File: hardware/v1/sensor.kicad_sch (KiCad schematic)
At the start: 22 parts, among them J10 Conn_01x03, J11 Conn_01x03, J3 Conn_01x03, J6 Conn_01x03, J7 Conn_01x03, J9 Conn_01x03, Q2 MMBT3904, U4 PCA9685BS, U5 BMI088, U7 BMP388

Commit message: some hardware designs
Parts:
- added C14, C15: 100n, Capacitor_SMD:C_0402_1005Metric, symbol Device:C
- added C15: 1u, Capacitor_SMD:C_0402_1005Metric, symbol Device:C
- added C26: 10n, Capacitor_SMD:C_0402_1005Metric, symbol Device:C_Small
- added J8: Conn_Coaxial, Connector_Coaxial:U.FL_Molex_MCRF_73412-0110_Vertical, symbol Connector:Conn_Coaxial
- added L1: L_Small, Inductor_SMD:L_0603_1608Metric, symbol Device:L_Small
- added R19: 10, Resistor_SMD:R_0402_1005Metric, symbol Device:R_Small
- added SW4: ACT/PASS, Button_Switch_SMD:SW_SPDT_PCM12, symbol Switch:SW_SPDT
- added U4: LIS3MDL, Package_LGA:LGA-12_2x2mm_P0.5mm, symbol Sensor_Magnetic:LIS3MDL
- added U8: NEO-M8N, RF_GPS:ublox_NEO, symbol RF_GPS:NEO-M8N
- U5: footprint LCSC:LGA-16_L4.5-W3.0-P0.50-BL -> ollyfc:PQFN50P450X300X100-16N
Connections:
- net +3V3: now also C15.1, C15.1, U4.5 (Vdd), U4.6 (Vdd_IO), U8.23 (VCC)
- net GND: now also C14.2, C15.2, C15.2, C26.2, J8.2 (Ext), U4.12 (GND), U4.2 (GND), U4.3 (GND), U8.10 (GND), U8.12 (GND), U8.13 (GND), U8.2 (D_SEL), U8.24 (GND), U8.7 (VDD_USB)
- net SPI2_MISO: now also U4.9 (SDO/SA1), U8.20 (TXD/SPI_MISO)
- net SPI2_MOSI: now also U4.11 (SDA/SDI/SDO), U8.21 (RXD/SPI_MOSI)
- net SPI2_SCK: now also U4.1 (SCL/SPC), U8.19 (SCL/SPI_CLK)
- new net: C26.1, L1.1, R19.2
- new net: C14.1, U4.4 (C1)
- new net: SW4.2 (B), U8.9 (VCC_RF)
- new net: R19.1, SW4.3 (C)
- new net GNSS_CS: U8.18 (SDA/~{SPI_CS})
- new net GNSS_INT: U8.4 (EXTINT)
- new net GNSS_RESET: U8.8 (~{RESET})
- new net GNSS_SAFEBOOT: U8.1 (~{SAFEBOOT})
- new net GNSS_TIMEP: U8.3 (TIMEPULSE)
- new net LNA_EN: U8.14 (LNA_EN)
- new net MAG_CS: U4.10 (~{CS})
- new net MAG_DRDY: U4.8 (DRDY)
- new net MAG_INT: U4.7 (INT)
- new net RF_IN: J8.1 (In), L1.2, U8.11 (RF_IN)
- new net VBAT: U8.22 (V_BCKP)
- no-connect marks 9 -> 11
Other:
- moved on the sheet: BZ1, C12, C13, C17, C18, D2, J10, J11, J3, J6, J7, J9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

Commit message: Route another?
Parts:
- removed SW4: ACT/PASS, Button_Switch_SMD:SW_SPDT_PCM12, symbol Switch:SW_SPDT
- added JP1: Jumper_2_Open, Connector_PinHeader_2.54mm:PinHeader_1x02_P2.54mm_Vertical, symbol Jumper:Jumper_2_Open
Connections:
- net CSB_ACCEL is gone; now on net +3V3: U5.14 (CSB1)
- net I2C3_SCL is gone; now on net I2C2_SCL: U4.23 (SCL)
- net I2C3_SDA is gone; now on net I2C2_SDA: U4.24 (SDA)
- net MAG_CS is gone; now on net +3V3: U4.10 (~{CS})
- net +3V3: now also U5.7 (PS)
- net 5VIN: now also BZ1.P (-); no longer BZ1.1 (-)
- net GND: now also U4.9 (SDO/SA1), U5.10 (SDO2), U5.15 (SDO1), U5.2 (NC); no longer U5.7 (PS), U8.2 (D_SEL)
- net SERVO_CH4: now also U4.15 (LED11); no longer U4.17 (LED13)
- net SERVO_CH5: now also U4.16 (LED12); no longer U4.18 (LED14)
- net SERVO_CH6: now also U4.17 (LED13); no longer U4.19 (LED15)
- net STATUS_A: now also U4.18 (LED14); no longer U4.9 (LED6)
- net STATUS_B: now also U4.19 (LED15); no longer U4.10 (LED7)
- net at C26.1, R19.2: now also JP1.2 (B); no longer L1.1
- net at U8.9 (VCC_RF): now also R19.1
- net at Q2.3 (C): now also BZ1.N (+); no longer BZ1.2 (+)
- net CSB_GYRO: no longer names the net of U5.5 (CSB2)
- net GNSS_CS renamed I2C1_SDA
- net I2C1_SDA: now also U4.11 (SDA/SDI/SDO), U5.9 (SDA/SDI)
- net LNA_EN: no longer names the net of U8.14 (LNA_EN)
- removed net SPI2_MISO: U4.9 (SDO/SA1), U5.10 (SDO2), U5.15 (SDO1), U8.20 (TXD/SPI_MISO)
- removed net SPI2_MOSI: U4.11 (SDA/SDI/SDO), U5.9 (SDA/SDI), U8.21 (RXD/SPI_MOSI)
- net SPI2_SCK renamed I2C1_SCL
- new net: JP1.1 (A), L1.1
- no-connect marks 11 -> 15
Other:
- moved on the sheet: C26, J10, J11, R19

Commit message: v2 PCB design
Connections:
- net VBAT is gone; now on net +3V3: U8.22 (V_BCKP)
- net I2C1_SCL: now also U7.2 (SCK); no longer U8.19 (SCL/SPI_CLK)
- net I2C1_SDA: now also U7.4 (SDI); no longer U8.18 (SDA/~{SPI_CS})
- net I2C2_SCL: now also U8.19 (SCL/SPI_CLK); no longer U7.2 (SCK)
- net I2C2_SDA: now also U8.18 (SDA/~{SPI_CS}); no longer U7.4 (SDI)
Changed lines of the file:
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@@
   (junction (at 32.385 162.56) (diameter 0) (color 0 0 0 0)
+  )
+  (junction (at 176.53 86.36) (diameter 0) (color 0 0 0 0)
   )
   (junction (at 82.55 45.72) (diameter 0) (color 0 0 0 0)
@@
     (stroke (width 0) (type default))
   )
-  (wire (pts (xy 179.07 89.535) (xy 179.07 77.47))
-    (stroke (width 0) (type default))
-  )
   (wire (pts (xy 79.375 134.62) (xy 69.85 134.62))
     (stroke (width 0) (type default))
@@
     (stroke (width 0) (type default))
   )
-  (wire (pts (xy 173.99 86.36) (xy 176.53 86.36))
-    (stroke (width 0) (type default))
-  )
   (wire (pts (xy 162.56 46.355) (xy 162.56 52.705))
     (stroke (width 0) (type default))
@@
     (stroke (width 0) (type default))
   )
+  (wire (pts (xy 179.07 89.535) (xy 179.07 86.36))
+    (stroke (width 0) (type default))
+  )
   (wire (pts (xy 258.445 27.94) (xy 256.54 27.94))
     (stroke (width 0) (type default))
@@
     (stroke (width 0) (type default))
   )
+  (wire (pts (xy 176.53 74.93) (xy 176.53 86.36))
+    (stroke (width 0) (type default))
+  )
   (wire (pts (xy 142.875 46.99) (xy 142.875 45.72))
     (stroke (width 0) (type default))
@@
     (stroke (width 0) (type default))
   )
-  (wire (pts (xy 179.07 77.47) (xy 175.895 77.47))
+  (wire (pts (xy 176.53 86.36) (xy 176.53 89.535))
     (stroke (width 0) (type default))
   )
@@
     (stroke (width 0) (type default))
   )
+  (wire (pts (xy 179.07 86.36) (xy 176.53 86.36))
+    (stroke (width 0) (type default))
+  )
   (wire (pts (xy 82.55 45.72) (xy 82.55 46.355))
     (stroke (width 0) (type default))
@@
   )
   (wire (pts (xy 242.57 41.91) (xy 248.92 41.91))
-    (stroke (width 0) (type default))
-  )
-  (wire (pts (xy 176.53 86.36) (xy 176.53 89.535))
     (stroke (width 0) (type default))
   )
@@
     )
   )
-  (global_label "I2C2_SDA" (shape input) (at 102.87 52.07 180) (fields_autoplaced)
+  (global_label "I2C1_SDA" (shape input) (at 102.87 52.07 180) (fields_autoplaced)
     (effects (font (size 1.27 1.27)) (justify right))
     (property "Intersheetrefs" "${INTERSHEET_REFS}" (at 91.0553 52.07 0)
@@
     )
   )
-  (global_label "I2C2_SCL" (shape input) (at 102.87 46.99 180) (fields_autoplaced)
+  (global_label "I2C1_SCL" (shape input) (at 102.87 46.99 180) (fields_autoplaced)
     (effects (font (size 1.27 1.27)) (justify right))
     (property "Intersheetrefs" "${INTERSHEET_REFS}" (at 91.1158 46.99 0)
@@
     )
   )
-  (global_label "I2C1_SDA" (shape input) (at 163.83 112.395 180) (fields_autoplaced)
+  (global_label "I2C2_SDA" (shape input) (at 163.83 112.395 180) (fields_autoplaced)
     (effects (font (size 1.27 1.27)) (justify right))
     (property "Intersheetrefs" "${INTERSHEET_REFS}" (at 152.0153 112.395 0)
@@
     )
   )
-  (global_label "I2C1_SCL" (shape input) (at 163.83 114.935 180) (fields_autoplaced)
+  (global_label "I2C2_SCL" (shape input) (at 163.83 114.935 180) (fields_autoplaced)
     (effects (font (size 1.27 1.27)) (justify right))
     (property "Intersheetrefs" "${INTERSHEET_REFS}" (at 152.0758 114.935 0)
-      (effects (font (size 1.27 1.27)) (justify right) hide)
-    )
-  )
-  (global_label "VBAT" (shape input) (at 175.895 77.47 180) (fields_autoplaced)
-    (effects (font (size 1.27 1.27)) (justify right))
-    (property "Intersheetrefs" "${INTERSHEET_REFS}" (at 168.495 77.47 0)
       (effects (font (size 1.27 1.27)) (justify right) hide)
     )
@@
       (effects (font (size 1.27 1.27)) (justify left))
     )
-    (property "Footprint" "ollyfc:PQFN50P450X300X100-16N" (at 53.34 72.39 0)
+    (property "Footprint" "ollyfc:PQFN50P450X300X100-16N" (at 53.34 59.69 0)
       (effects (font (size 1.27 1.27)))
     )
@@
     )
   )
-  (symbol (lib_id "power:+3V3") (at 173.99 86.36 0) (unit 1)
+  (symbol (lib_id "power:+3V3") (at 176.53 74.93 0) (unit 1)
     (in_bom yes) (on_board yes) (dnp no)
-    (property "Reference" "#PWR036" (at 173.99 90.17 0)
-      (effects (font (size 1.27 1.27)) hide)
-    )
-    (property "Value" "+3V3" (at 173.99 82.55 0)
+    (property "Reference" "#PWR036" (at 176.53 78.74 0)
+      (effects (font (size 1.27 1.27)) hide)
+    )
+    (property "Value" "+3V3" (at 176.53 71.12 0)
       (effects (font (size 1.27 1.27)))
     )
-    (property "Footprint" "" (at 173.99 86.36 0)
-      (effects (font (size 1.27 1.27)) hide)
-    )
-    (property "Datasheet" "" (at 173.99 86.36 0)
-      (effects (font (size 1.27 1.27)) hide)
-    )
+    (property "Footprint" "" (at 176.53 74.93 0)
+      (effects (font (size 1.27 1.27)) hide)
+    )
+    (property "Datasheet" "" (at 176.53 74.93 0)
+      (effects (font (size 1.27 1.27)) hide)
+    )

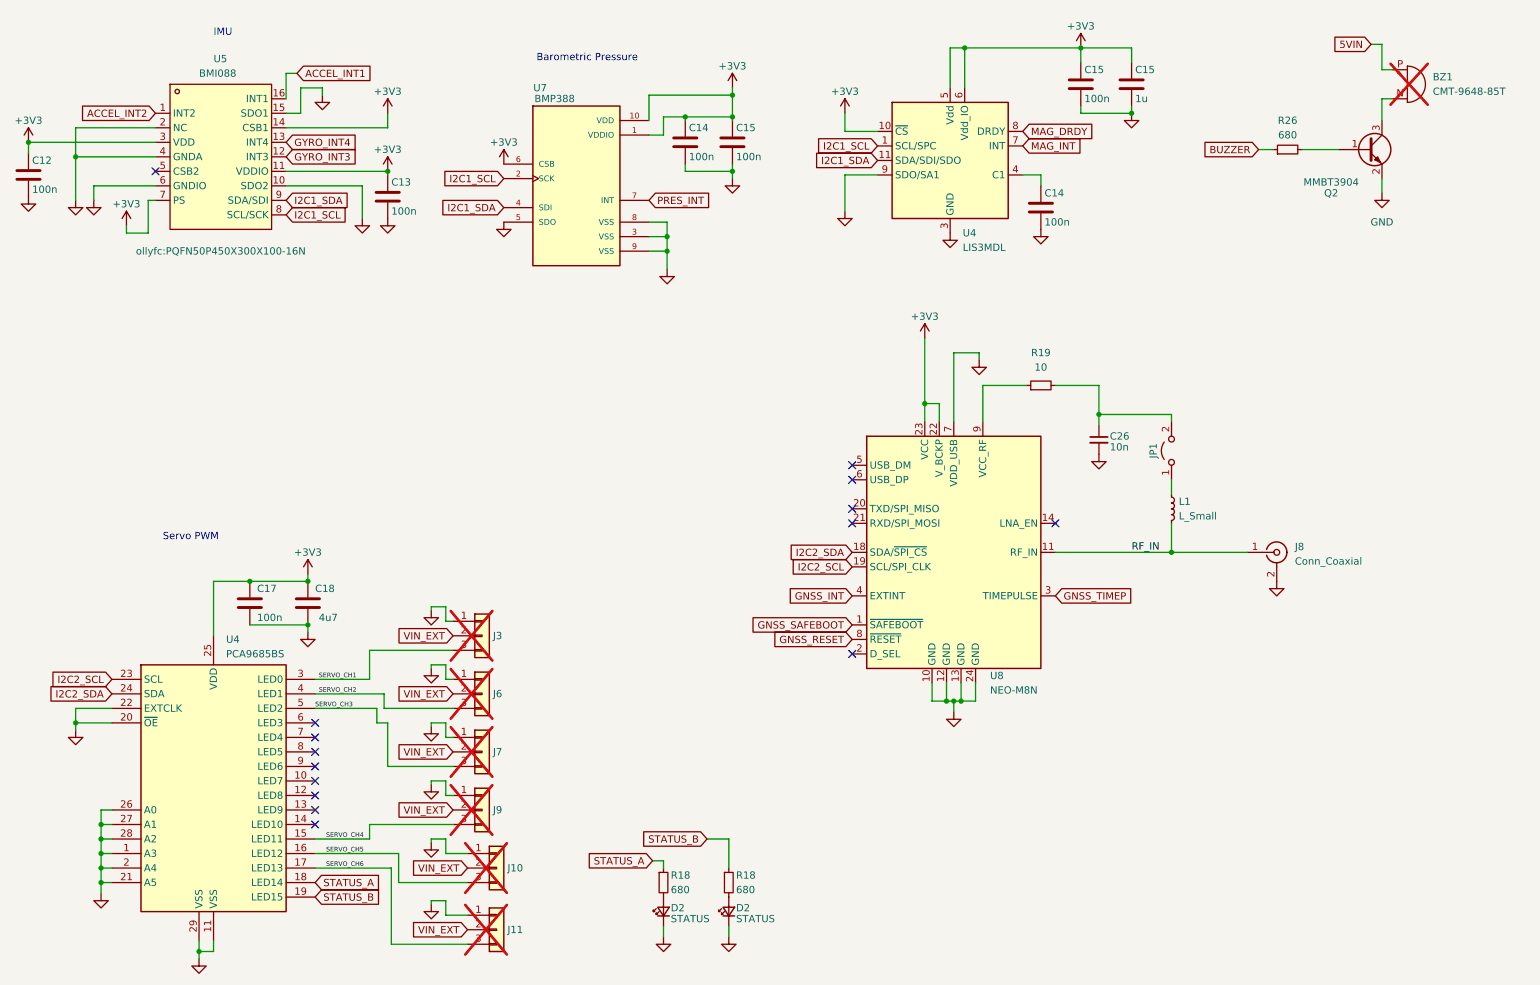
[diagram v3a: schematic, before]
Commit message: JLC part footprints
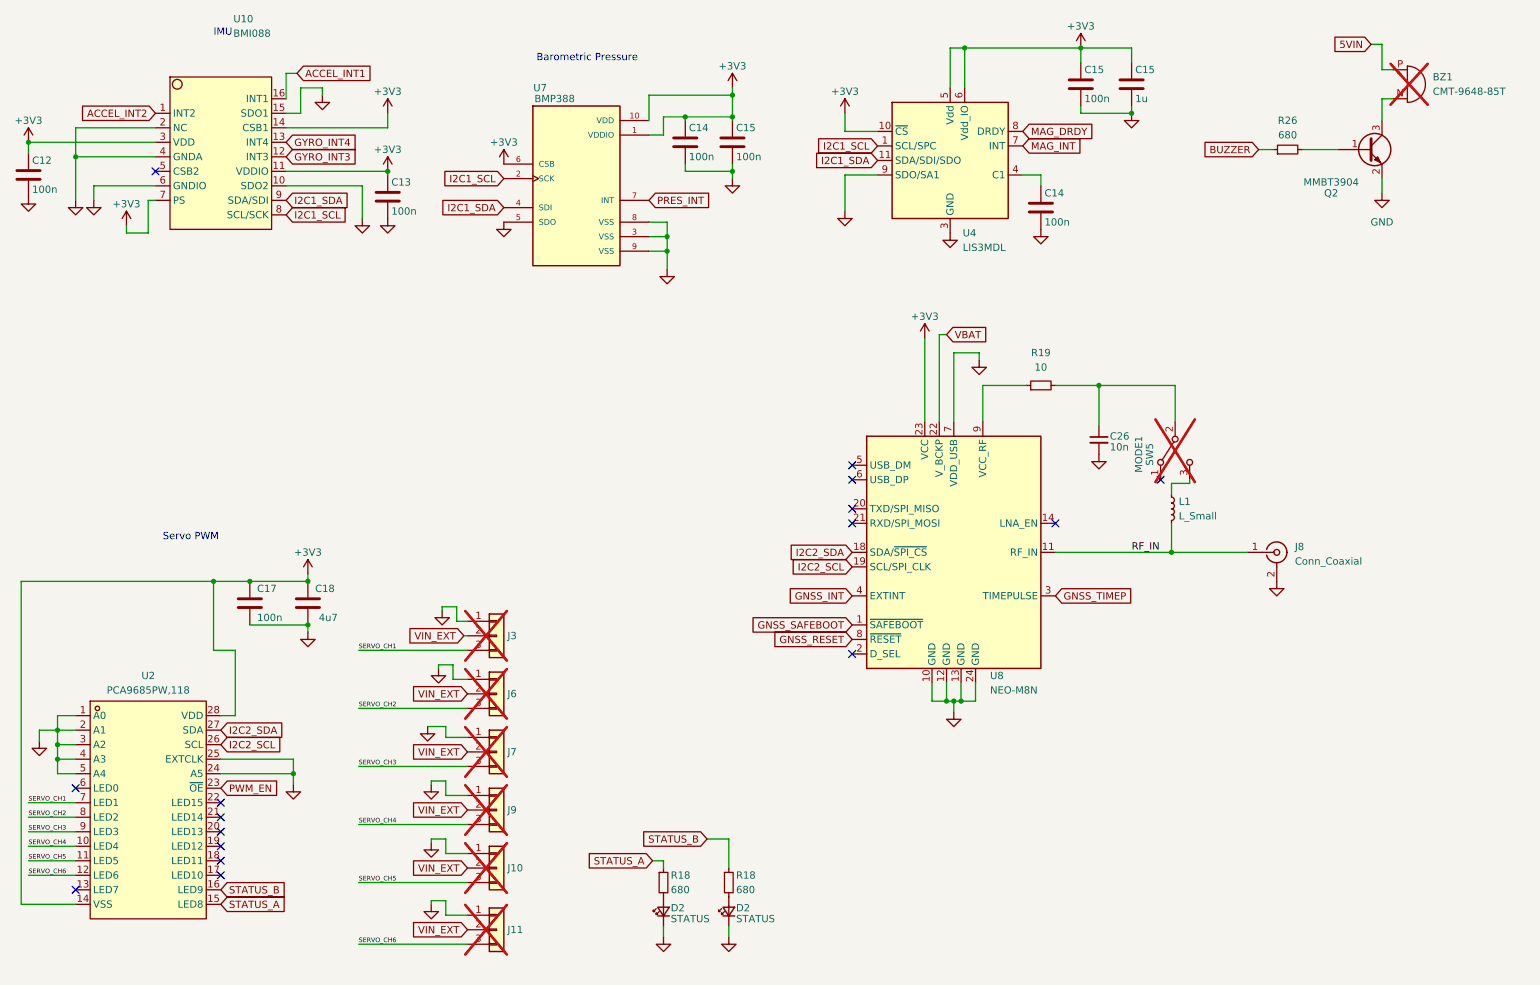
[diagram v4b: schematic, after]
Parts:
- removed JP1: Jumper_2_Open, Connector_PinHeader_2.54mm:PinHeader_1x02_P2.54mm_Vertical, symbol Jumper:Jumper_2_Open
- removed U4: PCA9685BS, Package_DFN_QFN:QFN-28-1EP_6x6mm_P0.65mm_EP4.25x4.25mm, symbol Driver_LED:PCA9685BS
- removed U5: BMI088, ollyfc:PQFN50P450X300X100-16N, symbol LCSC:BMI088
- added SW5: MODE1, Button_Switch_SMD:SW_SPDT_PCM12, symbol Switch:SW_SPDT
- added U10: BMI088, ofc_sym:LGA-16_L4.5-W3.0-P0.50-BL, symbol ofc_sym:BMI088
- added U2: PCA9685PW,118, ofc_sym:TSSOP-28_L9.7-W4.4-P0.65-LS6.4-TL, symbol ofc_sym:PCA9685PW,118
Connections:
- net +3V3: now also U10.11 (VDDIO), U10.14 (CSB1), U10.3 (VDD), U10.7 (PS), U2.14 (VSS), U2.28 (VDD); no longer U8.22 (V_BCKP)
- net ACCEL_INT1: now also U10.16 (INT1)
- net ACCEL_INT2: now also U10.1 (INT2)
- net GND: now also U10.10 (SDO2), U10.15 (SDO1), U10.2 (NC), U10.4 (GNDA), U10.6 (GNDIO), U2.1 (A0), U2.2 (A1), U2.24 (A5), U2.25 (EXTCLK), U2.3 (A2), U2.4 (A3), U2.5 (A4)
- net GYRO_INT3: now also U10.12 (INT3)
- net GYRO_INT4: now also U10.13 (INT4)
- net I2C1_SCL: now also U10.8 (SCL/SCK)
- net I2C1_SDA: now also U10.9 (SDA/SDI)
- net I2C2_SCL: now also U2.26 (SCL)
- net I2C2_SDA: now also U2.27 (SDA)
- net SERVO_CH1: now also U2.7 (LED1)
- net SERVO_CH2: now also U2.8 (LED2)
- net SERVO_CH3: now also U2.9 (LED3)
- net SERVO_CH4: now also U2.10 (LED4)
- net SERVO_CH5: now also U2.11 (LED5)
- net SERVO_CH6: now also U2.12 (LED6)
- net STATUS_A: now also U2.15 (LED8)
- net STATUS_B: now also U2.16 (LED9)
- net at L1.1: now also SW5.3 (C)
- net at C26.1, R19.2: now also SW5.2 (B)
- new net PWM_EN: U2.23 (~{OE})
- new net VBAT: U8.22 (V_BCKP)
- no-connect marks 15 -> 16
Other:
- moved on the sheet: J3, J6, J7, J9
